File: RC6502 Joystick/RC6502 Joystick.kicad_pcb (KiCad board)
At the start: 2 copper layers, 99.1 x 61.6 mm, 44 parts, among them J1 Atari_Joystick, J2 Port, J3 Base, J4 RC6502_Backplane, SW1 SW_Push, SW2 SW_Push, SW3 SW_Push, SW4 SW_Push, SW5 SW_Push, SW6 SW_Push, SW7 SW_Push, SW8 SW_Push, U1 74LS245, U2 74LS373, U3 74LS138, U4 74LS138

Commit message: Gerber export
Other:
- board text added: "RC6502 Digital I/O & Joystick Revision A"
- board text removed: "RC6502 Digital I/O Revision A"
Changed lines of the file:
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@@
   (gr_line (start 175.26 103.505) (end 175.26 96.52) (angle 90) (layer Edge.Cuts) (width 0.15))
   (gr_line (start 164.465 94.615) (end 173.355 94.615) (angle 90) (layer Edge.Cuts) (width 0.15))
-  (gr_text "RC6502\nDigital I/O\nRevision A" (at 111.76 124.46) (layer F.SilkS)
+  (gr_text "RC6502\nDigital I/O\n& Joystick\nRevision A" (at 112.395 124.46) (layer F.SilkS)
     (effects (font (size 1.5 1.5) (thickness 0.3)))
   )

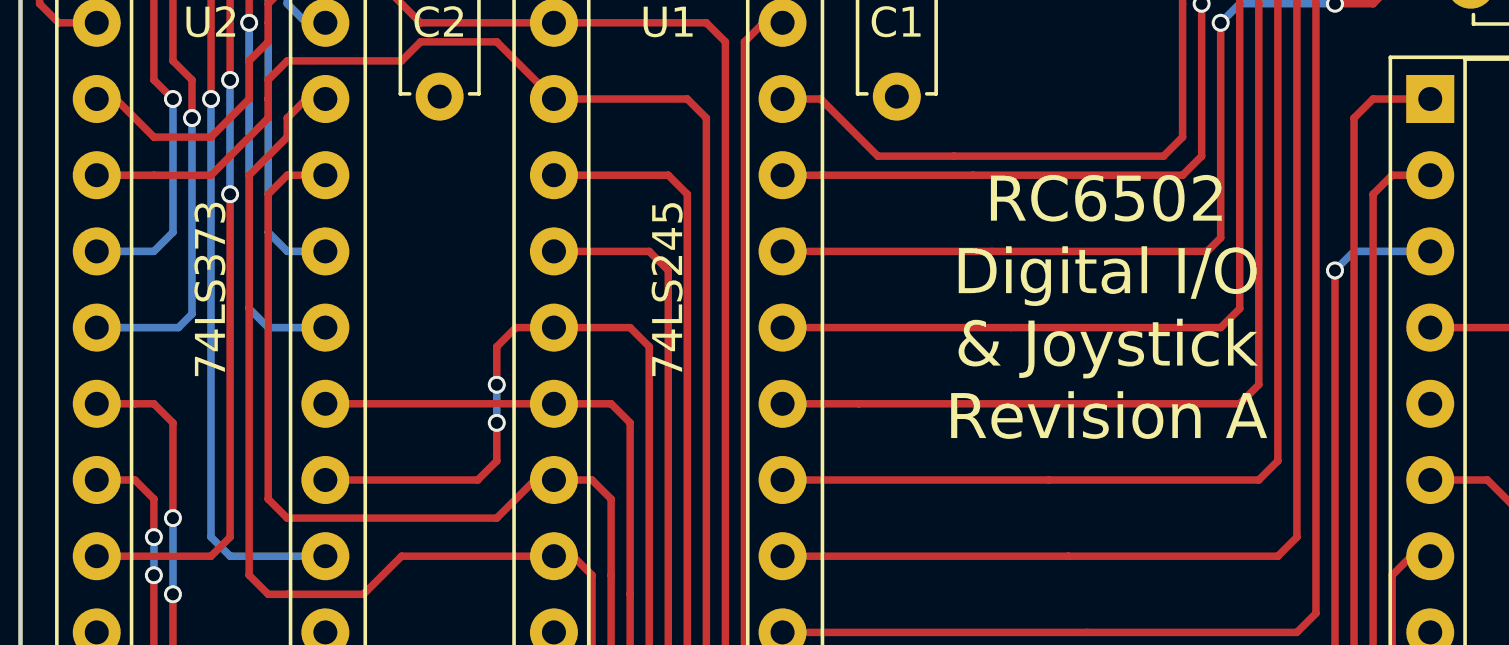
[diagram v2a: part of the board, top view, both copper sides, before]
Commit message: Accidentally put 74LS373 instead of 74LS374
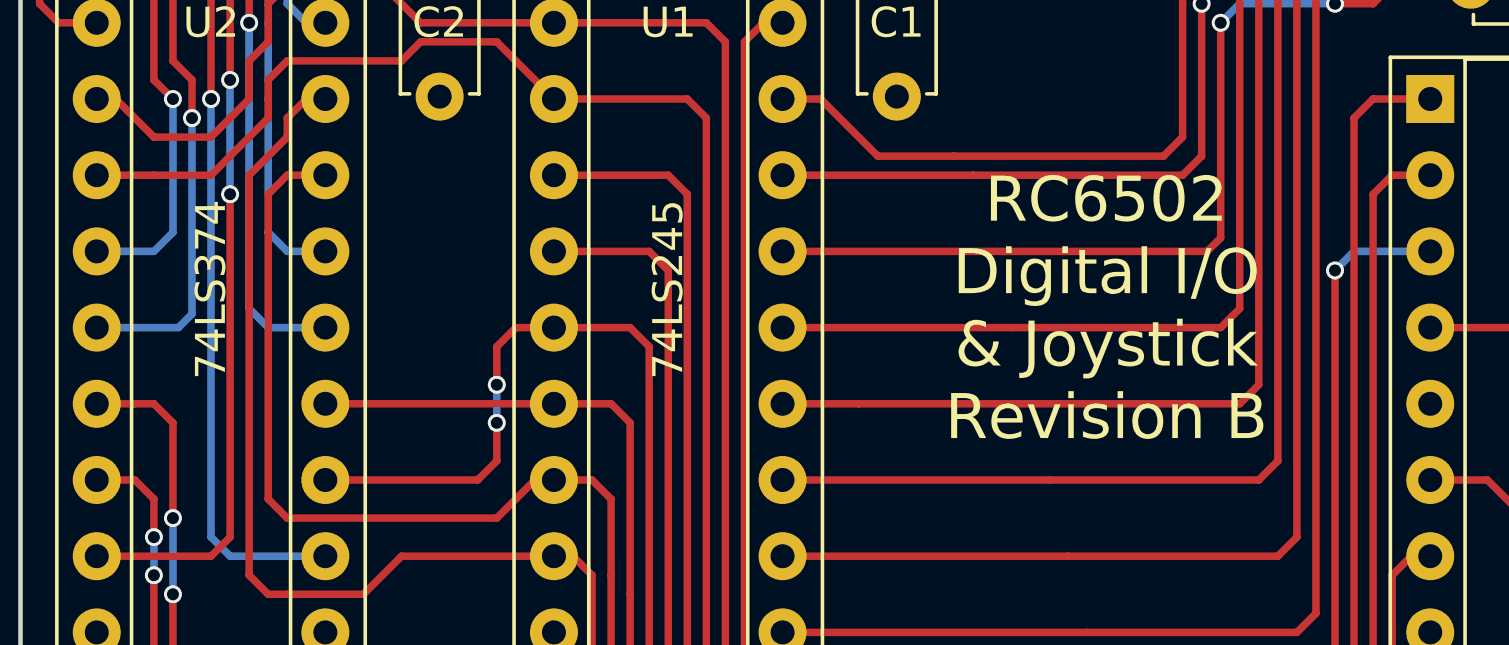
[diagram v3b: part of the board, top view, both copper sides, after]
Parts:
- U2: value 74LS373 -> 74LS374
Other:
- board text added: "RC6502 Digital I/O & Joystick Revision B"
- board text removed: "RC6502 Digital I/O & Joystick Revision A"
